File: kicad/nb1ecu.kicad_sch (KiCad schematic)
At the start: 2 parts, among them P2 178780-1, U1 Teensy4.1

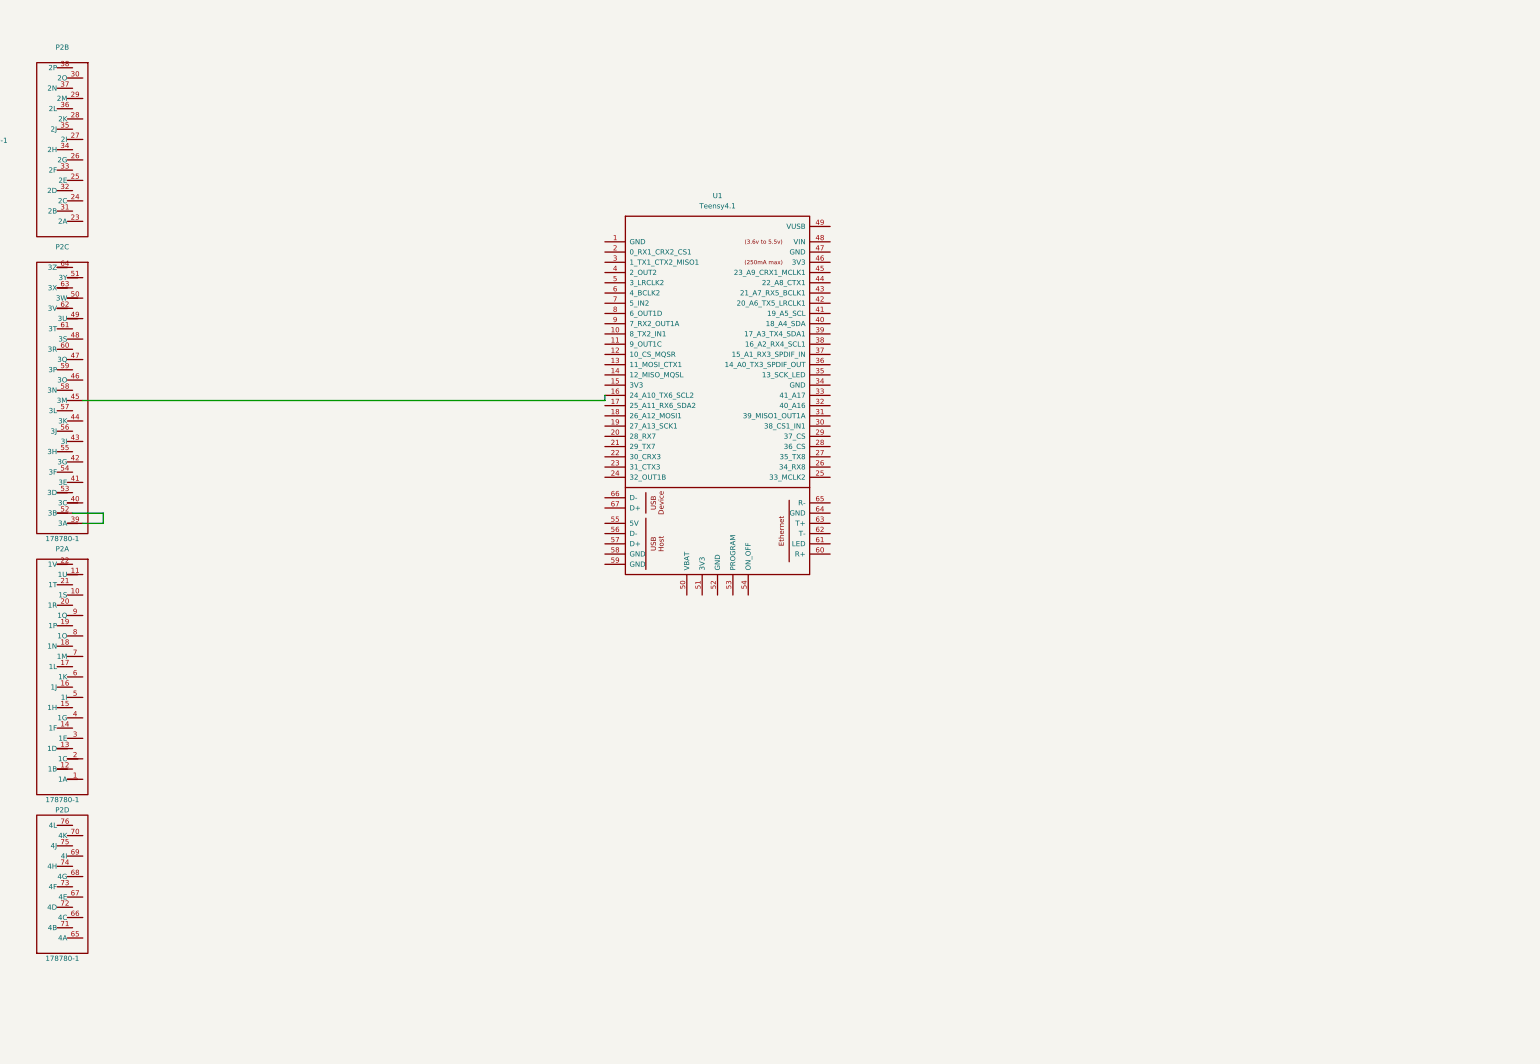
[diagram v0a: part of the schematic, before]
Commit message: ready to test, need to add part numbers for bom
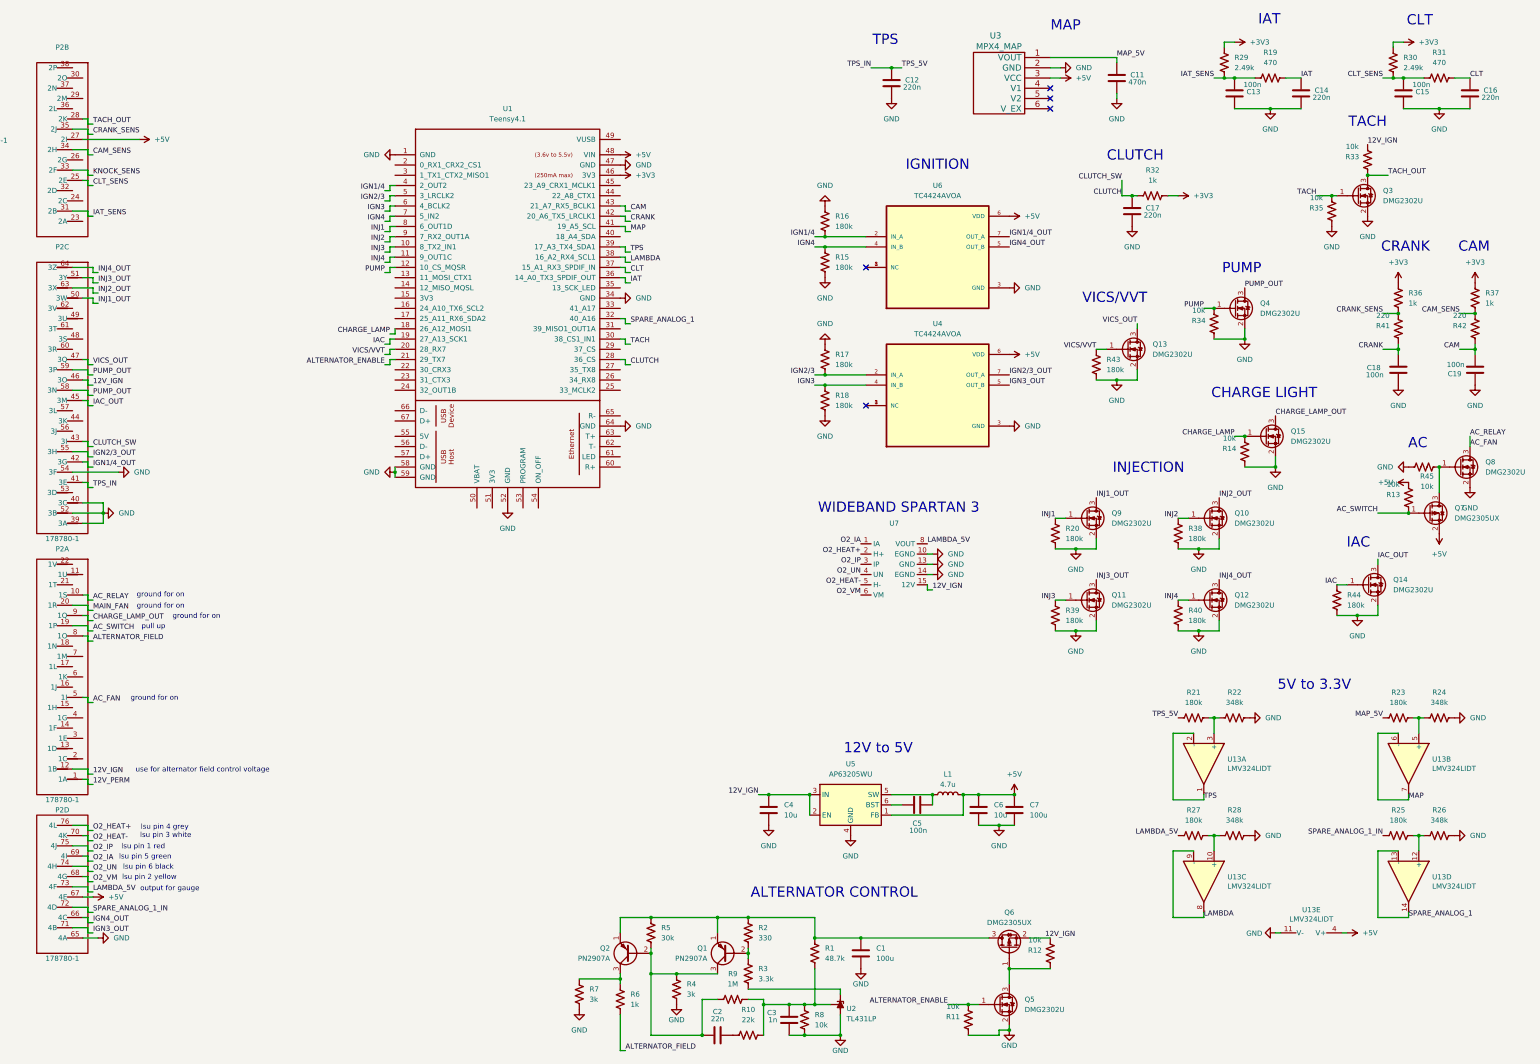
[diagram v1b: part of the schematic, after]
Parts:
- added C1, C7: 100u, Capacitor_THT:CP_Radial_D6.3mm_P2.50mm, symbol Device:C
- added C11: 470n, Capacitor_SMD:C_0805_2012Metric_Pad1.18x1.45mm_HandSolder, symbol Device:C
- added C12, C14, C16, C17: 220n, Capacitor_SMD:C_0805_2012Metric_Pad1.18x1.45mm_HandSolder, symbol Device:C
- added C13, C15, C18, C19, C5: 100n, Capacitor_SMD:C_0805_2012Metric_Pad1.18x1.45mm_HandSolder, symbol Device:C
- added C2: 22n, Capacitor_SMD:C_0805_2012Metric_Pad1.18x1.45mm_HandSolder, symbol Device:C
- added C3: 1n, Capacitor_SMD:C_0805_2012Metric_Pad1.18x1.45mm_HandSolder, symbol Device:C
- added C4, C6: 10u, Capacitor_SMD:C_0805_2012Metric_Pad1.18x1.45mm_HandSolder, symbol Device:C
- added L1: 4.7u, Inductor_SMD:L_1008_2520Metric_Pad1.43x2.20mm_HandSolder, symbol Device:L
- added Q1, Q2: PN2907A, Package_TO_SOT_THT:TO-92_Inline_Wide, symbol Transistor_BJT:2N3905
- added Q10, Q11, Q12, Q13, Q14, Q15, Q3, Q4, Q5, Q8, Q9: DMG2302U, Package_TO_SOT_SMD:SOT-23, symbol Transistor_FET:DMG2302U
- added Q6, Q7: DMG2305UX, Package_TO_SOT_SMD:SOT-23, symbol Transistor_FET:Q_PMOS_GSD
- added R1: 48.7k, Resistor_SMD:R_0805_2012Metric_Pad1.20x1.40mm_HandSolder, symbol Device:R_US
- added R10: 22k, Resistor_SMD:R_0805_2012Metric_Pad1.20x1.40mm_HandSolder, symbol Device:R_US
- added R11, R12, R13, R14, R33, R34, R35, R45, R8: 10k, Resistor_SMD:R_0805_2012Metric_Pad1.20x1.40mm_HandSolder, symbol Device:R_US
- added R15, R16, R17, R18, R20, R21, R23, R25, R27, R38, R39, R40, R43, R44: 180k, Resistor_SMD:R_0805_2012Metric_Pad1.20x1.40mm_HandSolder, symbol Device:R_US
- added R19, R31: 470, Resistor_SMD:R_0805_2012Metric_Pad1.20x1.40mm_HandSolder, symbol Device:R_US
- added R2: 330, Resistor_SMD:R_0805_2012Metric_Pad1.20x1.40mm_HandSolder, symbol Device:R_US
- added R22, R24, R26, R28: 348k, Resistor_SMD:R_0805_2012Metric_Pad1.20x1.40mm_HandSolder, symbol Device:R_US
- added R29, R30: 2.49k, Resistor_SMD:R_0805_2012Metric_Pad1.20x1.40mm_HandSolder, symbol Device:R_US
- added R3: 3.3k, Resistor_SMD:R_0805_2012Metric_Pad1.20x1.40mm_HandSolder, symbol Device:R_US
- added R32, R36, R37, R6: 1k, Resistor_SMD:R_0805_2012Metric_Pad1.20x1.40mm_HandSolder, symbol Device:R_US
- added R4, R7: 3k, Resistor_SMD:R_0805_2012Metric_Pad1.20x1.40mm_HandSolder, symbol Device:R_US
- added R41, R42: 220, Resistor_SMD:R_0805_2012Metric_Pad1.20x1.40mm_HandSolder, symbol Device:R_US
- added R5: 30k, Resistor_SMD:R_0805_2012Metric_Pad1.20x1.40mm_HandSolder, symbol Device:R_US
- added R9: 1M, Resistor_SMD:R_0805_2012Metric_Pad1.20x1.40mm_HandSolder, symbol Device:R_US
- added U13: LMV324LIDT, Package_SO:SOIC-14_3.9x8.7mm_P1.27mm, symbol Amplifier_Operational:LMV324
- added U2: TL431LP, Package_TO_SOT_THT:TO-92_Inline, symbol Reference_Voltage:TL431LP
- added U3: MPX4_MAP, mpx:MPX-4_MAP, symbol MPX-4_MAP:MPX4_MAP
- added U4, U6: TC4424AVOA, TC4424AVOA:SOIC127P599X175-8N, symbol TC4424AVOA:TC4424AVOA
- added U5: AP63205WU, Package_TO_SOT_SMD:TSOT-23-6, symbol Regulator_Switching:AP63205WU
- added U7: ~, spartan3oem:spartan3oem, symbol spartan3oem:spartan3oem
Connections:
- net CLT_SENS: now reaches P2.25 (2E)
- net CLT_SENS: now also C15.1, R30.2, R31.2
- net +5V: now reaches P2.27 (2I)
- net +5V: now also P2.67 (4E), U1.48 (VIN), C6.1, C7.1, L1.2, Q7.2 (S), R13.1, U13.4 (V+), U3.3 (VCC), U4.6 (VDD), U5.1 (FB), U6.6 (VDD)
- net TACH_OUT: now reaches P2.28 (2K)
- net TACH_OUT: now also Q3.3 (D), R33.2
- net IAT_SENS: now reaches P2.31 (2B)
- net IAT_SENS: now also C13.1, R19.2, R29.2
- net KNOCK_SENS: now reaches P2.33 (2F)
- net CAM_SENS: now reaches P2.34 (2H)
- net CAM_SENS: now also R37.1, R42.1
- net CRANK_SENS: now reaches P2.35 (2J)
- net CRANK_SENS: now also R36.1, R41.1
- net GND: now reaches U1.1 (GND)
- net GND: now also P2.39 (3A), P2.40 (3C), P2.52 (3B), P2.54 (3F), P2.65 (4A), U1.34 (GND), U1.47 (GND), U1.52 (GND), U1.58 (GND), U1.59 (GND), U1.64 (GND), C1.2, C11.2, C12.2, C13.2, C14.2, C15.2, C16.2, C17.2, C18.1, C19.1, C3.1, C4.2, C6.2, C7.2, Q10.2 (S), Q11.2 (S), Q12.2 (S), Q13.2 (S), Q14.2 (S), Q15.2 (S), Q3.2 (S), Q4.2 (S), Q5.2 (S), Q8.2 (S), Q9.2 (S), R11.2, R14.2, R15.1, R16.2, R17.2, R18.1, R20.1, R22.2, R24.2, R26.2, R28.2, R34.2, R35.2, R38.1, R39.1, R4.2, R40.1, R43.1, R44.1, R45.1, R7.2, R8.2, U13.11 (V-), U2.2 (A), U3.2 (GND), U4.3 (GND), U5.4 (GND), U6.3 (GND), U7.10 (EGND), U7.13 (GND), U7.14 (EGND)
- net INJ3: now reaches U1.10 (8_TX2_IN1)
- net INJ3: now also Q11.1 (G), R39.2
- net INJ4: now reaches U1.11 (9_OUT1C)
- net INJ4: now also Q12.1 (G), R40.2
- net PUMP: now reaches U1.12 (10_CS_MQSR)
- net PUMP: now also Q4.1 (G), R34.1
- net at U1.16 (24_A10_TX6_SCL2): no longer P2.45 (3M)
- net CHARGE_LAMP: now reaches U1.18 (26_A12_MOSI1)
- net CHARGE_LAMP: now also Q15.1 (G), R14.1
- net IAC: now reaches U1.19 (27_A13_SCK1)
- net IAC: now also Q14.1 (G), R44.2
- net VICS/VVT: now reaches U1.20 (28_RX7)
- net VICS/VVT: now also Q13.1 (G), R43.2
- net ALTERNATOR_ENABLE: now reaches U1.21 (29_TX7)
- net ALTERNATOR_ENABLE: now also Q5.1 (G), R11.1
- net CLUTCH: now reaches U1.28 (36_CS)
- net CLUTCH: now also P2.43 (3I), C17.1, R32.1
- net TACH: now reaches U1.30 (38_CS1_IN1)
- net TACH: now also Q3.1 (G), R35.1
- net SPARE_ANALOG_1: now reaches U1.32 (40_A16)
- net SPARE_ANALOG_1: now also U13.13 (-), U13.14
- net IAT: now reaches U1.36 (14_A0_TX3_SPDIF_OUT)
- net IAT: now also C14.1, R19.1
- net CLT: now reaches U1.37 (15_A1_RX3_SPDIF_IN)
- net CLT: now also C16.1, R31.1
- net LAMBDA: now reaches U1.38 (16_A2_RX4_SCL1)
- net LAMBDA: now also U13.8, U13.9 (-)
- net TPS: now reaches U1.39 (17_A3_TX4_SDA1)
- net TPS: now also U13.1, U13.2 (-)
- net IGN1/4: now reaches U1.4 (2_OUT2)
- net IGN1/4: now also R16.1, U6.2 (IN_A)
- net MAP: now reaches U1.41 (19_A5_SCL)
- net MAP: now also U13.6 (-), U13.7
- net CRANK: now reaches U1.42 (20_A6_TX5_LRCLK1)
- net CRANK: now also C18.2, R41.2
- net CAM: now reaches U1.43 (21_A7_RX5_BCLK1)
- net CAM: now also C19.2, R42.2
- net +3V3: now reaches U1.46 (3V3)
- net +3V3: now also R29.1, R30.1, R32.2, R36.2, R37.2
- net IGN2/3: now reaches U1.5 (3_LRCLK2)
- net IGN2/3: now also R17.1, U4.2 (IN_A)
- net IGN3: now reaches U1.6 (4_BCLK2)
- net IGN3: now also R18.2, U4.4 (IN_B)
- net IGN4: now reaches U1.7 (5_IN2)
- net IGN4: now also R15.2, U6.4 (IN_B)
- net INJ1: now reaches U1.8 (6_OUT1D)
- net INJ1: now also Q9.1 (G), R20.2
- net INJ2: now reaches U1.9 (7_RX2_OUT1A)
- net INJ2: now also Q10.1 (G), R38.2
- net IGN4_OUT: now reaches P2.66 (4C)
- net IGN4_OUT: now also U6.5 (OUT_B)
- net O2_VM: now reaches P2.68 (4G)
- net O2_VM: now also U7.6 (VM)
- net O2_IA: now reaches P2.69 (4I)
- net O2_IA: now also U7.1 (IA)
- net O2_HEAT-: now reaches P2.70 (4K)
- net O2_HEAT-: now also U7.5 (H-)
- net IGN3_OUT: now reaches P2.71 (4B)
- net IGN3_OUT: now also U4.5 (OUT_B)
- net SPARE_ANALOG_1_IN: now reaches P2.72 (4D)
- net SPARE_ANALOG_1_IN: now also R25.1
- net LAMBDA_5V: now reaches P2.73 (4F)
- net LAMBDA_5V: now also R27.1, U7.8 (VOUT)
- net O2_UN: now reaches P2.74 (4H)
- net O2_UN: now also U7.4 (UN)
- net O2_IP: now reaches P2.75 (4J)
- net O2_IP: now also U7.3 (IP)
- net O2_HEAT+: now reaches P2.76 (4L)
- net O2_HEAT+: now also U7.2 (H+)
- net 12V_PERM: now reaches P2.1 (1A)
- net AC_FAN: now reaches P2.10 (1S)
- net AC_FAN: now also P2.5 (1I), Q8.3 (D)
- net 12V_IGN: now reaches P2.12 (1B)
- net 12V_IGN: now also P2.46 (3O), C4.1, Q6.2 (S), R12.1, R33.1, U5.2 (EN), U5.3 (IN), U7.15 (12V)
- net AC_SWITCH: now reaches P2.19 (1P)
- net AC_SWITCH: now also Q7.1 (G), R13.2
- net MAIN_FAN: now reaches P2.20 (1R)
- net ALTERNATOR_FIELD: now reaches P2.8 (1O)
- net ALTERNATOR_FIELD: now also R6.2
- net CHARGE_LAMP_OUT: now reaches P2.9 (1Q)
- net CHARGE_LAMP_OUT: now also Q15.3 (D)
- net TPS_5V: now reaches P2.41 (3E)
- net TPS_5V: now also C12.1, R21.1
- net IGN1/4_OUT: now reaches P2.42 (3G)
- net IGN1/4_OUT: now also U6.7 (OUT_A)
- net VICS_OUT: now reaches P2.47 (3Q)
- net VICS_OUT: now also Q13.3 (D)
- net INJ1_OUT: now reaches P2.50 (3W)
- net INJ1_OUT: now also Q9.3 (D)
- net INJ3_OUT: now reaches P2.51 (3Y)
- net INJ3_OUT: now also Q11.3 (D)
- net IGN2/3_OUT: now reaches P2.55 (3H)
- net IGN2/3_OUT: now also U4.7 (OUT_A)
- net PUMP_OUT: now reaches P2.58 (3N)
- net PUMP_OUT: now also P2.59 (3P), Q4.3 (D)
- net INJ2_OUT: now reaches P2.63 (3X)
- net INJ2_OUT: now also Q10.3 (D)
- net INJ4_OUT: now reaches P2.64 (3Z)
- net INJ4_OUT: now also Q12.3 (D)
- new net: R21.2, R22.1, U13.3 (+)
- new net: R23.2, R24.1, U13.5 (+)
- new net: R27.2, R28.1, U13.10 (+)
- new net: R25.2, R26.1, U13.12 (+)
- new net: C1.1, Q1.1 (E), Q2.1 (E), Q6.3 (D), R1.1, R2.1, R5.1
- new net: C2.1, Q1.3 (C), Q2.2 (B), R4.1, R5.2, R9.1
- new net: Q2.3 (C), R6.1, R7.1
- new net: C5.1, L1.1, U5.5 (SW)
- new net: C5.2, U5.6 (BST)
- new net: C3.2, R1.2, R10.2, R8.1, R9.2, U2.1 (REF)
- new net: Q7.3 (D), Q8.1 (G), R45.2
- new net: C2.2, R10.1
- new net: Q5.3 (D), Q6.1 (G), R12.2
- new net: Q1.2 (B), R2.2, R3.1
- new net: R3.2, U2.3 (K)
- new net: U4.1 (NC), U4.8 (NC)
- new net: U6.1 (NC), U6.8 (NC)
- new net IAC_OUT: P2.45 (3M), Q14.3 (D)
- new net MAP_5V: C11.1, R23.1, U3.1 (VOUT)
- no-connect marks 0 -> 5
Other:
- note added: "12V to 5V"
- note added: "5V to 3.3V"
- note added: "AC"
- note added: "ALTERNATOR CONTROL"
- note added: "CAM"
- note added: "CHARGE LIGHT"
- note added: "CLT"
- note added: "CLUTCH"
- note added: "CRANK"
- note added: "IAC"
- note added: "IAT"
- note added: "IGNITION"
- note added: "INJECTION"
- note added: "MAP"
- note added: "PUMP"
- note added: "TACH"
- note added: "TPS"
- note added: "VICS/VVT"
- note added: "WIDEBAND SPARTAN 3"
- note added: "ground for on"
- note added: "lsu pin 1 red"
- note added: "lsu pin 2 yellow"
- note added: "lsu pin 3 white"
- note added: "lsu pin 4 grey"
- note added: "lsu pin 5 green"
- note added: "lsu pin 6 black"
- note added: "output for gauge"
- note added: "pull up"
- note added: "use for alternator field control voltage"
- moved on the sheet: U1

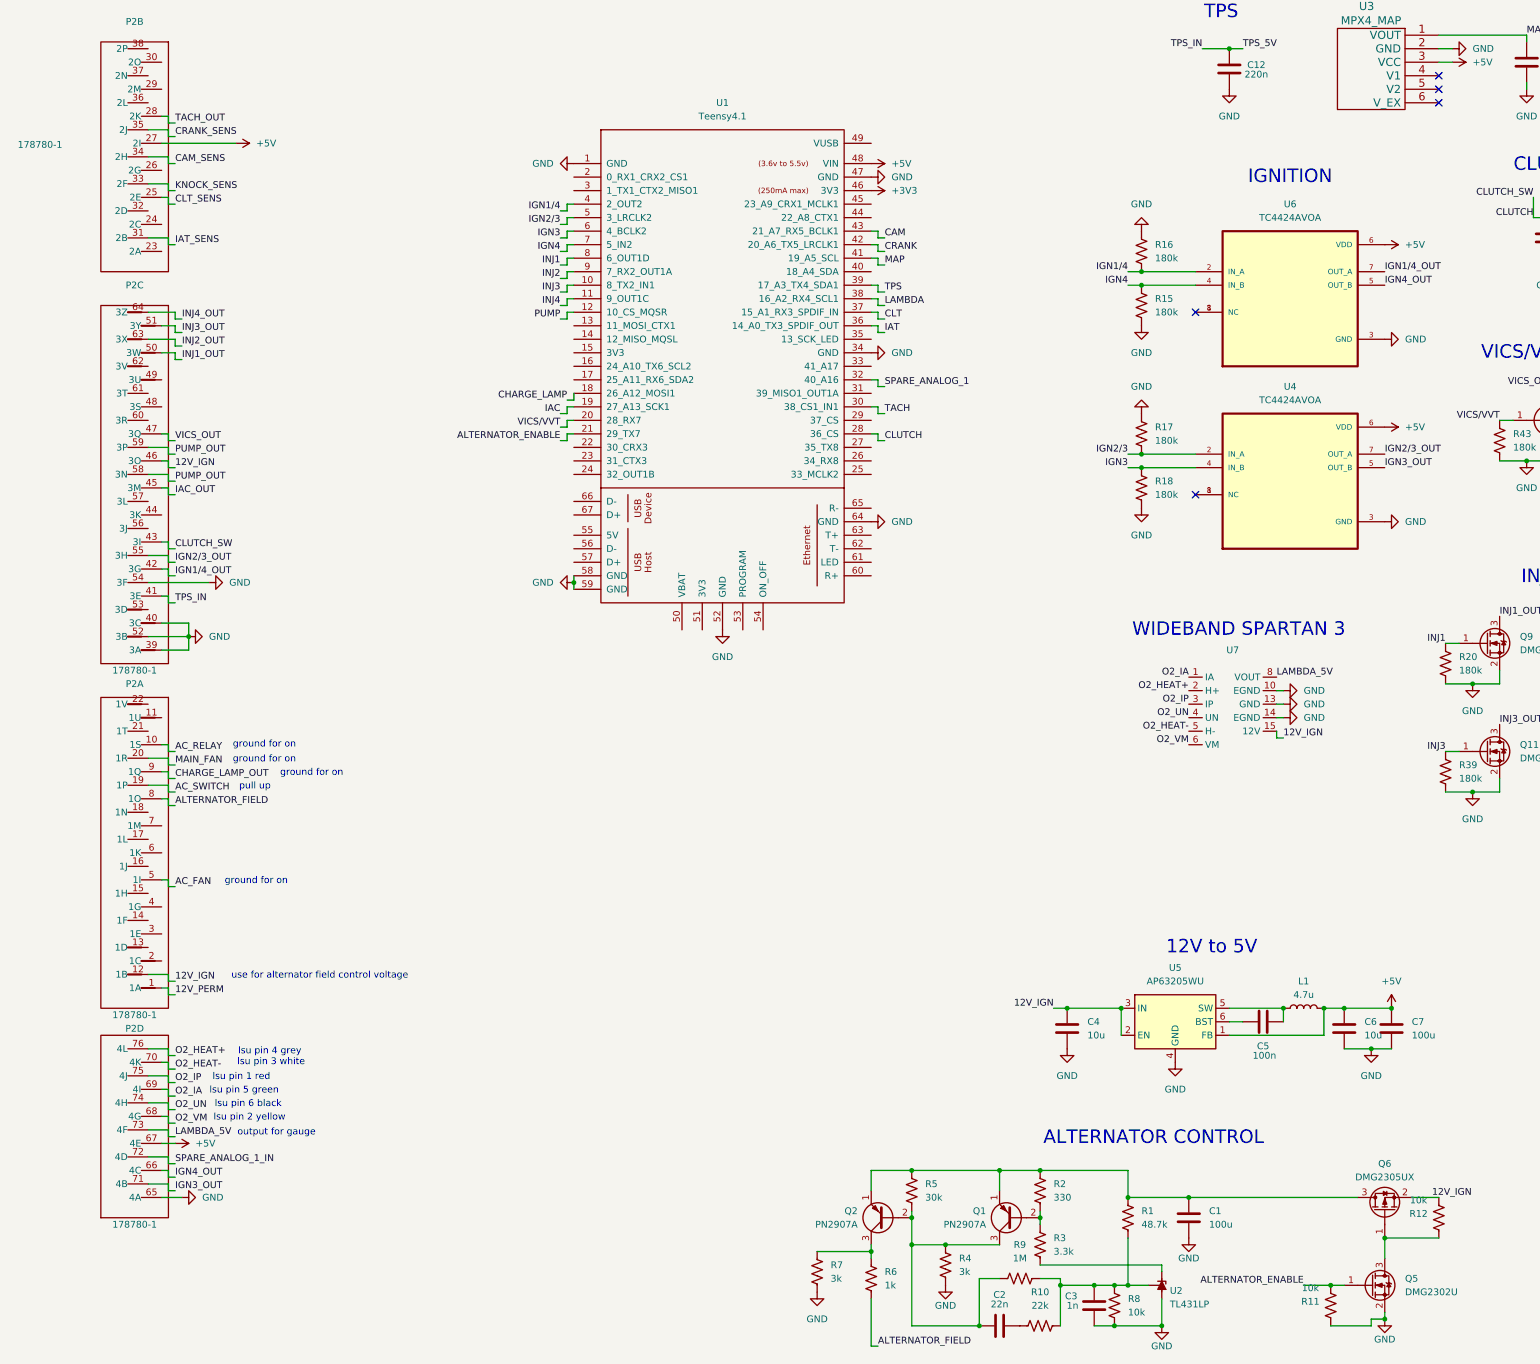
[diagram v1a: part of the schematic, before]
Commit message: boost control instead of lambda output on connector and other fixes
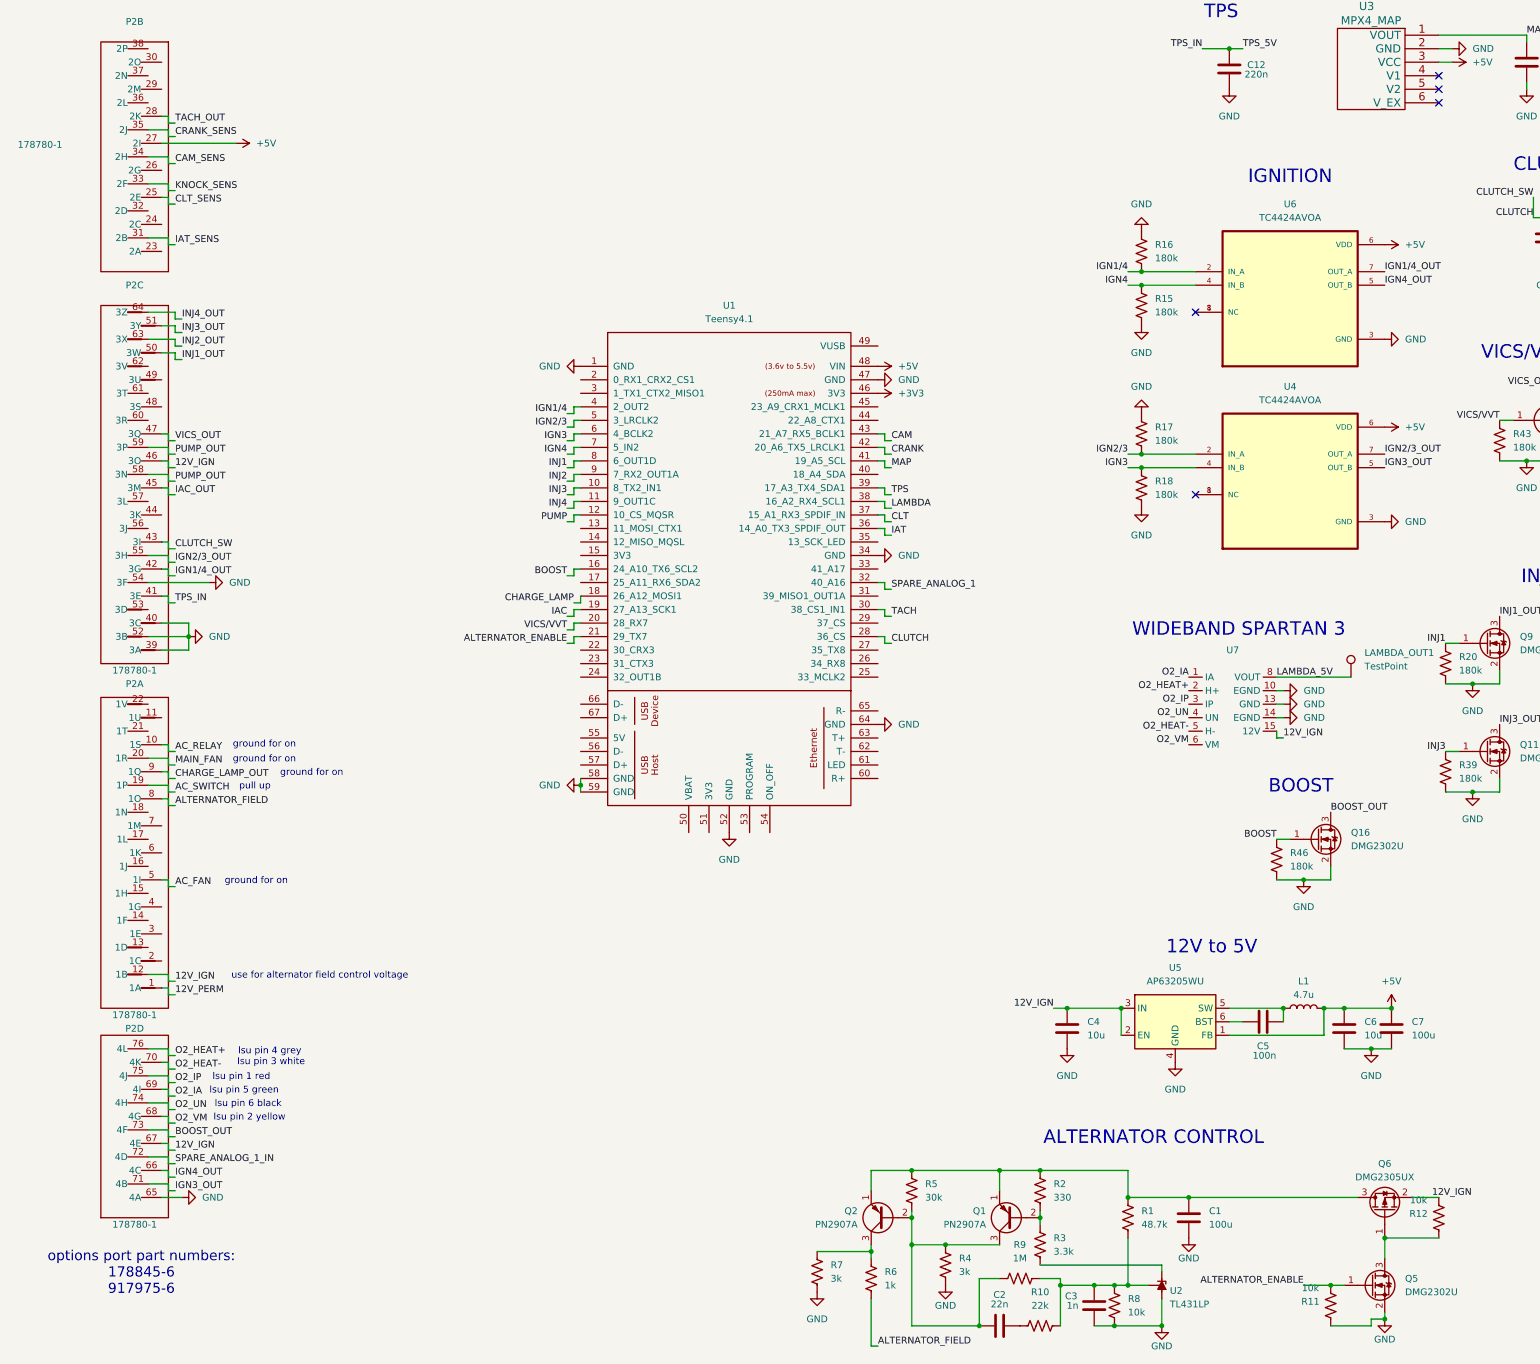
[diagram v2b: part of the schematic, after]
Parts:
- added LAMBDA_OUT1: TestPoint, TestPoint:TestPoint_Pad_3.0x3.0mm, symbol Connector:TestPoint
- added Q16: DMG2302U, Package_TO_SOT_SMD:SOT-23, symbol Transistor_FET:DMG2302U
- added R46: 180k, Resistor_SMD:R_0805_2012Metric_Pad1.20x1.40mm_HandSolder, symbol Device:R_US
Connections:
- net +5V: no longer P2.67 (4E)
- net 12V_IGN: now also P2.67 (4E)
- net GND: now also Q16.2 (S), R46.1
- net LAMBDA_5V: now also LAMBDA_OUT1.1; no longer P2.73 (4F)
- net BOOST: now reaches U1.16 (24_A10_TX6_SCL2)
- net BOOST: now also Q16.1 (G), R46.2
- new net BOOST_OUT: P2.73 (4F), Q16.3 (D)
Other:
- note added: "BOOST"
- note added: "options port part numbers: 178845-6 917975-6"
- note removed: "output for gauge"
- moved on the sheet: U1
